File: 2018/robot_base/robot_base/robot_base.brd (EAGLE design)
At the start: 92.5 x 74.4 mm, 41 parts

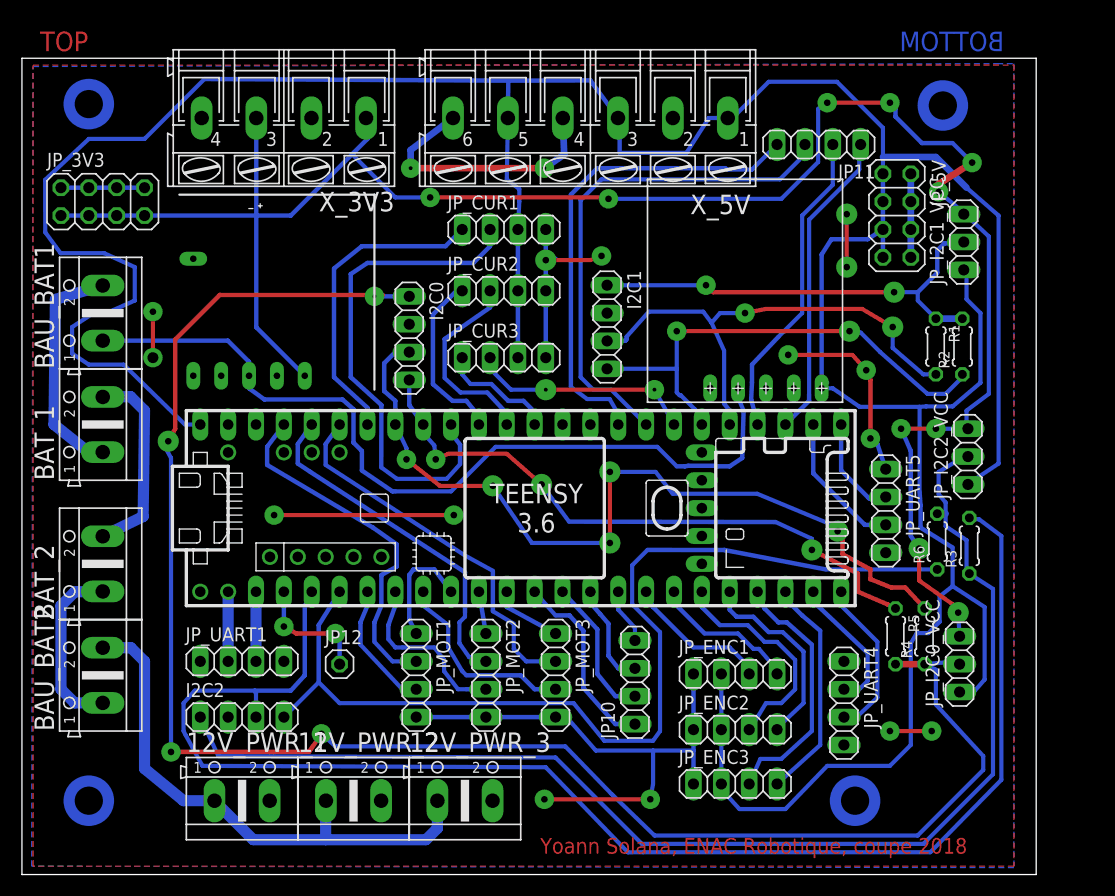
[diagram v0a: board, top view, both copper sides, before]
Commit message: [robot_base] Increase clearance. Better routing.
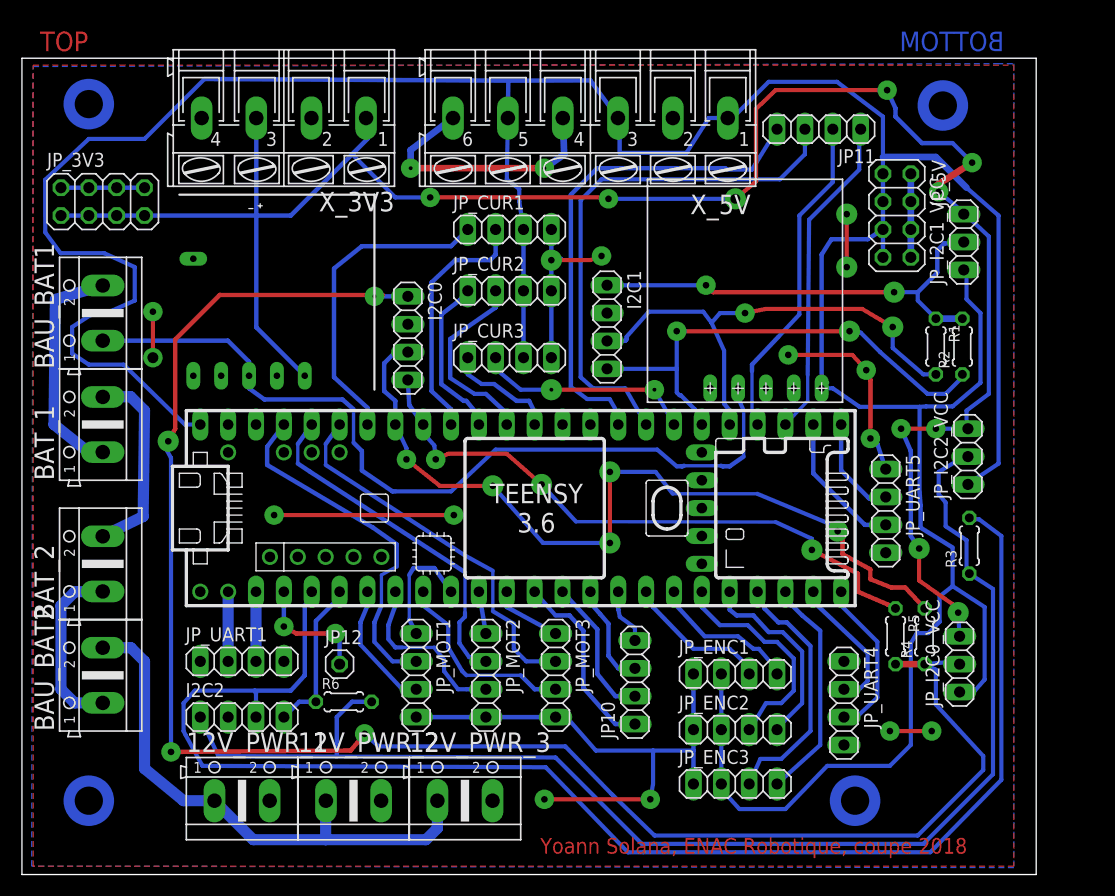
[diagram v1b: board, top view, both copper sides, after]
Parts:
- moved R6 56.0 mm to (38.5, 15.4), turned to 0 degrees
- moved JP11 1.40 mm to (81.8, 67.6)
- moved JP_CUR1 0.51 mm to (53.6, 58.4)
- moved JP_CUR2 0.51 mm to (53.6, 52.8)
- moved JP_CUR3 0.51 mm to (53.6, 46.7)
- moved I2C0 0.13 mm to (44.3, 48.5)
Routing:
- net SDA2: track 92.1 -> 14.4 mm
- net CUR1_SE: track 46.0 -> 22.9 mm
- net I2C2_VCC: track 114.3 -> 120.9 mm
- net 3V3: track 182.0 -> 184.3 mm
- net N$53: track 47.0 -> 48.9 mm
- net N$57: track 28.6 -> 30.1 mm
- net N$58: track 28.4 -> 29.6 mm
- net CUR2_NF: track 16.1 -> 15.0 mm
- net N$52: track 45.2 -> 46.3 mm
- net CUR2_SE: track 18.1 -> 17.4 mm
- net CUR3_SE: track 20.4 -> 19.8 mm
- net CUR3_NF: track 10.7 -> 10.2 mm
- net SCL0: track 76.3 -> 75.8 mm
- net CUR1_NF: track 28.6 -> 29.1 mm
- net GND: track 173.4 -> 172.9 mm
